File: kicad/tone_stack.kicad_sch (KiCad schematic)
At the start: 5 parts

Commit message: Tone stack: Bass + Treble (passive James) with a switchable mid cut (errata #20)
The panel has Bass and Treble pots, but the design carried a single treble-cut
"Tone" substitute -- and the recovered preamp coupling was the 470 pF chime cap
alone, a 1.3 kHz high-pass that passed no bass at all. Replace both:

- C_cpl_out 1 uF full-band coupling from Q2's drain; C_treble 470 pF becomes a
  bright cap across the top of the volume pot.
- Passive James (Thomas-Vox) Bass/Treble network -- the originals' topology,
  asymmetric, more cut than boost, kept over an active Baxandall so the amp
  keeps its character -- driven by a TL074 (IC3: input buffer, x2 make-up,
  gyrator, output buffer) on its own mid-rail VBIAS_3. Both pots 250k lin in
  the original holes.
- MID CUT toggle for honky pickups: R_mid + a switched series-resonant gyrator
  shunt (1.86 H simulated + 22 nF): -9.6 dB at ~800 Hz, Q ~0.6, flat when off,
  no DC across the switch. SW_MID sits in the original line-reverse switch
  hole -- no new panel holes.
- SPICE: ac_tonestack.cir rewritten rail-aware (all IC3 nodes 8.50 V, noon
  -0.21 dB, notch -9.65 dB at 796 Hz); sweep_tonestack.cir sweeps both pots
  and the switch; results committed.

Generator / placer / router:
- OPAMP14 and SW_SPST symbols, VB_3 / TMK test points (28), BOM rows for IC3,
  the DIP-14 socket, POT_BASS/POT_TREB, SW_MID.
- gen_pcb: tighter profiles (THT 1.2 mm gap / 3.5 mm channels, SMD 0.4 mm),
  overflow repair by moving width between columns, small parts kept in
  schematic order on the shelves, tone/preamp column weighted wider, TP cells
  6x4.5 with the courtyard flush to the cell, input-jack pads down the LEFT
  edge on the 155x90 board (the bottom edge is ~9 mm short for 13 groups),
  keepout rule areas (2 mm edge frame + M3 hole squares) exported to the
  router.
- route_board: refuse a board without its .kicad_pro (a copy routed away from
  the project came back with 0.2 mm tracks and 400 DRC errors); prune
  zero-length segments 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
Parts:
- removed C_cut: 10nF, Capacitor_THT:C_Disc_D7.5mm_W2.5mm_P5.00mm, symbol cr_primitives:C
- removed POT_TONE: 100k lin, cambridge_reverb:WirePad_1x03_P2.54mm_D1.2mm, symbol cr_primitives:POT
- added C_byp3: 100nF, Capacitor_THT:C_Disc_D7.5mm_W2.5mm_P5.00mm, symbol cr_primitives:C
- added C_gg: 1.8nF, Capacitor_THT:C_Disc_D7.5mm_W2.5mm_P5.00mm, symbol cr_primitives:C
- added C_j1, C_j2, C_res: 22nF, Capacitor_THT:C_Disc_D7.5mm_W2.5mm_P5.00mm, symbol cr_primitives:C
- added C_j3, C_j4: 2.2nF, Capacitor_THT:C_Disc_D7.5mm_W2.5mm_P5.00mm, symbol cr_primitives:C
- added C_tout: 1uF, Capacitor_THT:C_Disc_D7.5mm_W2.5mm_P5.00mm, symbol cr_primitives:C
- added C_treble: 470pF, Capacitor_THT:C_Disc_D7.5mm_W2.5mm_P5.00mm, symbol cr_primitives:C
- added C_vb3: 47uF/25V, Capacitor_THT:CP_Radial_D6.3mm_P2.50mm, symbol cr_primitives:CP
- added IC3: TL074CN, Package_DIP:DIP-14_W7.62mm, symbol cr_primitives:OPAMP14
- added POT_BASS, POT_TREB: 250k lin, cambridge_reverb:WirePad_1x03_P2.54mm_D1.2mm, symbol cr_primitives:POT
- added R_gL: 4.7k, Resistor_THT:R_Axial_DIN0207_L6.3mm_D2.5mm_P5.08mm_Vertical, symbol cr_primitives:R
- added R_gg: 220k, Resistor_THT:R_Axial_DIN0207_L6.3mm_D2.5mm_P5.08mm_Vertical, symbol cr_primitives:R
- added R_inb: 1M, Resistor_THT:R_Axial_DIN0207_L6.3mm_D2.5mm_P5.08mm_Vertical, symbol cr_primitives:R
- added R_j1, R_j2, R_mid, R_mk1, R_mk2: 10k, Resistor_THT:R_Axial_DIN0207_L6.3mm_D2.5mm_P5.08mm_Vertical, symbol cr_primitives:R
- added R_j3: 68k, Resistor_THT:R_Axial_DIN0207_L6.3mm_D2.5mm_P5.08mm_Vertical, symbol cr_primitives:R
- added R_j4: 1k, Resistor_THT:R_Axial_DIN0207_L6.3mm_D2.5mm_P5.08mm_Vertical, symbol cr_primitives:R
- added R_vb31, R_vb32: 100k, Resistor_THT:R_Axial_DIN0207_L6.3mm_D2.5mm_P5.08mm_Vertical, symbol cr_primitives:R
- added SW_MID: MID CUT, cambridge_reverb:WirePad_1x02_P2.54mm_D1.2mm, symbol cr_primitives:SW_SPST
- added TP_MK_OUT: TMK, cambridge_reverb:TestPoint_THT_D2.0mm_Label, symbol cr_primitives:TP
- added TP_VBIAS_3: VB_3, cambridge_reverb:TestPoint_THT_D2.0mm_Label, symbol cr_primitives:TP
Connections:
- net GND: now also C_byp3.2, C_vb3.2, IC3.11 (V-), R_vb32.2
- net PREAMP_OUT: now also IC3.3 (IN1+), R_inb.1; no longer POT_VOL.1
- net TONE_OUT: now also C_treble.2
- new net +17V: C_byp3.1, IC3.4 (V+), R_vb31.1
- new net BUF: C_j3.1, IC3.1 (OUT1), IC3.2 (IN1-), R_j1.1
- new net GYA: C_gg.1, C_res.2, R_gL.1
- new net GYO: IC3.8 (OUT3), IC3.9 (IN3-), R_gL.2
- new net GYP: C_gg.2, IC3.10 (IN3+), R_gg.1
- new net JA: C_j1.1, POT_BASS.3, R_j1.2
- new net JB: C_j2.2, POT_BASS.1, R_j2.1
- new net JOUT: IC3.5 (IN2+), R_j3.2, R_j4.2
- new net JTA: C_j3.2, POT_TREB.3
- new net JTB: C_j4.1, POT_TREB.1
- new net JWB: C_j1.2, C_j2.1, POT_BASS.2 (W), R_j3.1
- new net JWT: POT_TREB.2 (W), R_j4.1
- new net MID: IC3.12 (IN4+), R_mid.2, SW_MID.1
- new net MIDSW: C_res.1, SW_MID.2
- new net MKN: IC3.6 (IN2-), R_mk1.2, R_mk2.1
- new net MK_OUT: IC3.7 (OUT2), R_mid.1, R_mk1.1, TP_MK_OUT.1
- new net OBUF: C_tout.1, IC3.13 (IN4-), IC3.14 (OUT4)
- new net VBIAS_3: C_j4.2, C_vb3.1 (+), R_gg.2, R_inb.2, R_j2.2, R_mk2.2, R_vb31.2, R_vb32.1, TP_VBIAS_3.1
- new net VOLTOP: C_tout.2, C_treble.1, POT_VOL.1
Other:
- note added: "TONE -- IC3 TL074. A: input buffer. PASSIVE JAMES bass/treble network (the Thomas-Vox topology: panel Bass + Treble pots; ~flat at noon with a slight bright tilt, bass +-6 dB @100 Hz, treble +6/-16 dB @10 kHz -- more cut than boost, as the originals). B: make-up gain x2 (network loss). C: gyrator MID CUT (-10 dB @ ~790 Hz, Q~0.6, SW_MID toggle in the line-reverse hole). D: output buffer -> Volume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"
- note removed: "TONE -- Volume + passive Vox 'cut' (treble). DESIGNED SUBSTITUTE: original 25-5274-2 tone values not recovered (cross-check #4); response verified in spice/ac_tonestack.cir. Original panel may have had separate Treble/Bass."

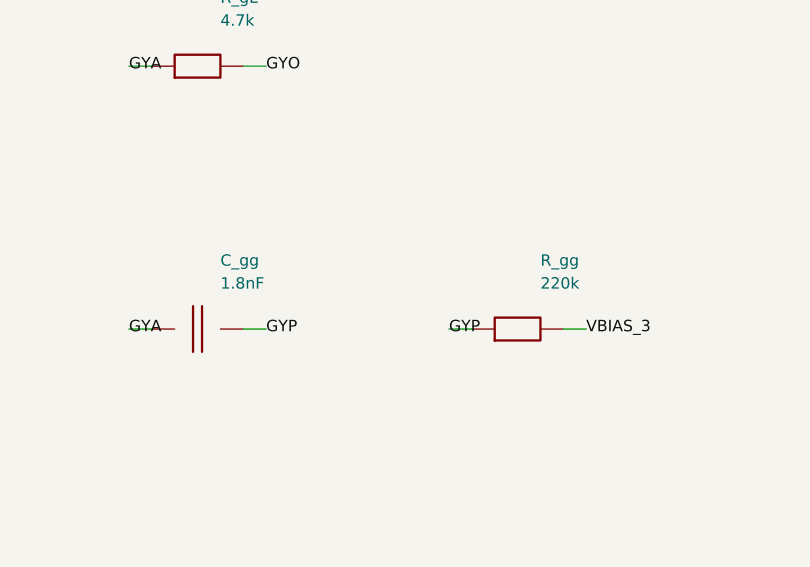
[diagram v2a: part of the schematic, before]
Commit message: Noise, hum, crosstalk and thermal models; three design fixes; JLCPCB rules and cost
New models (docs/06c, spice/): a .noise run of the whole front end including the
LM317's own rail noise, the rail-ripple paths to the speaker, a vactrol-level tremolo
depth model, an electro-thermal LM1875 ladder, and a geometric crosstalk audit of the
routed boards (kicad/gen/crosstalk_audit.py). They found three defects:

- Errata #21 (hum + hiss): the LM1875 bias divider had no bypass (+4 dB ripple to
  speaker, 0.4 Vrms of 100 Hz at idle) and the LM317's 0.5 mV of noise reached the
  0 dB-PSRR JFET stages (23 dB above their floor, SNR 34 dB). Fixed with C_bref +
  R_bias3 on the power amp, C_adj on the regulator, and an RC-decoupled +17V_PRE rail
  for Q1/Q2/Q_rec: hum 408 mV -> 0.3 mV, EIN 37 -> 2.7 uV, SNR 34 -> 57 dB.
- Errata #22 (tremolo depth 1.7 dB): the vactrol LED was returned to ground from a
  mid-rail LFO -> 7 mA DC, a fixed -20 dB pad. LED limiter (2 V swing, LED_rate is one
  limiter LED) + Q_trem 2N3904/MMBT3904 emitter follower AC-coupled from the depth
  pot -> 15 dB depth, 0.8 dB insertion loss.
- Errata #23 (fab): stock TO-92 and the LM1875 footprint were under JLCPCB's 0.18 mm
  annular-ring minimum -> TO-92_Inline_Wide and 1.5 mm LM1875 pads; both .kicad_pro
  carry JLC's 2-layer limits as DRC constraints. Cost: all SMD caps 1206 (basic
  library), "(opt)" MRB caps DNP, gyrator on E24 values (same 1.86 H): 7 -> 2
  extended part types, ~$32 -> ~$17 assembly for five boards (kicad/gen/jlc_cost.py);
  three fiducials on the SMD board.

Crosstalk -> two routing rules (.kicad_dru: HighCurrent 0.6/0.4 mm and TankDrive
1.2/0.8 mm from signal copper, THT/SMD) that route_board.py also hands the router as
class clearances; keepout rule areas along the edge and around the mounting holes.
Thermal: Part 5's <= 2.5 K/W heatsink confirmed with numbers (Tj 97 C at 40 C ambient,
worst-case sine; 8-10 K/W clip-ons reach shutdown).

Placer: short parts stack beside tall ones i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
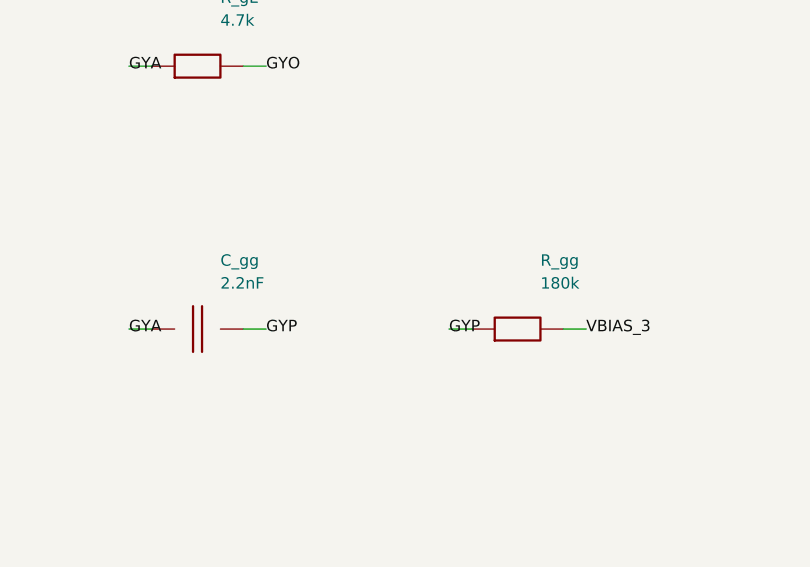
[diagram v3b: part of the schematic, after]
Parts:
- C_gg: value 1.8nF -> 2.2nF
- R_gg: value 220k -> 180k
